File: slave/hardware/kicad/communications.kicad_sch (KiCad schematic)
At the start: 18 parts, among them IC8 L9616, Q2 BSS138, Q3 BSS138, Q4 BSS138, Q5 BSS138

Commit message: feat(HW): add USB Type-C interface
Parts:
- added J1: USB_C_Receptacle_USB2.0_16P, Connector_USB:USB_C_Receptacle_HCTL_HC-TYPE-C-16P-01A, symbol Datalogger:USB_C_Receptacle_USB2.0_16P
- added R71, R73, R74: 20kR, Resistor_SMD:R_0603_1608Metric, symbol Device:R
- added R72: 10kR, Resistor_SMD:R_0603_1608Metric, symbol Device:R
- renumbered C50 to C56, C51 to C57, IC8 to IC12, R11 to R60, R10 to R61, R14 to R62, R15 to R63, R12 to R64, R13 to R65, R16 to R66, R17 to R67, R98 to R68, R99 to R69, R100 to R70
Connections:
- net GNDREF: now also J1.A1 (GND), J1.A12 (GND), J1.B1 (GND), J1.B12 (GND), R71.1, R73.1, R74.1
- new net: J1.A5 (CC1), R73.2
- new net: J1.B5 (CC2), R71.2
- new net: J1.A4 (VBUS), J1.A9 (VBUS), J1.B4 (VBUS), J1.B9 (VBUS), R72.1
- new net USB_D_N: J1.A7 (D-), J1.B7 (D-)
- new net USB_D_P: J1.A6 (D+), J1.B6 (D+)
- new net VBUS: R72.2, R74.2
- no-connect marks 1 -> 4
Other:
- moved on the sheet: C56, C57, IC12, R68, R69, R70

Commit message: feat(HW): add footprints and configure component properties
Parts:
- C56, C57: footprint (none) -> Capacitor_SMD:C_0201_0603Metric
- IC12: footprint SOIC127P600X175-8N -> Datalogger:SOIC127P600X175-8N
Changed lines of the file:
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@@
 			)
 		)
-		(property "Footprint" ""
+		(property "Footprint" "Capacitor_SMD:C_0201_0603Metric"
 			(at 135.89 62.23 0)
 			(hide yes)
@@
 			)
 		)
-		(property "Footprint" ""
+		(property "Footprint" "Capacitor_SMD:C_0201_0603Metric"
 			(at 81.28 49.53 0)
 			(hide yes)
@@
 			)
 		)
-		(property "Footprint" "SOIC127P600X175-8N"
+		(property "Footprint" "Datalogger:SOIC127P600X175-8N"
 			(at 114.3 46.99 0)
 			(hide yes)

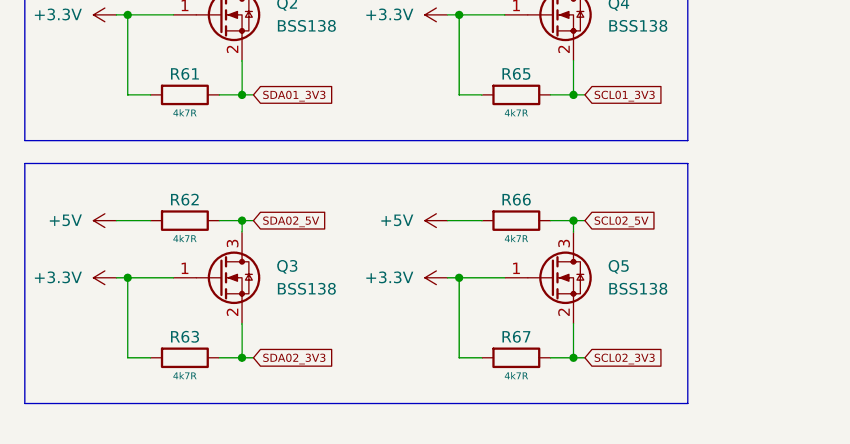
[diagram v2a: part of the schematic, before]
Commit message: feat(HW): add initial schematic pages
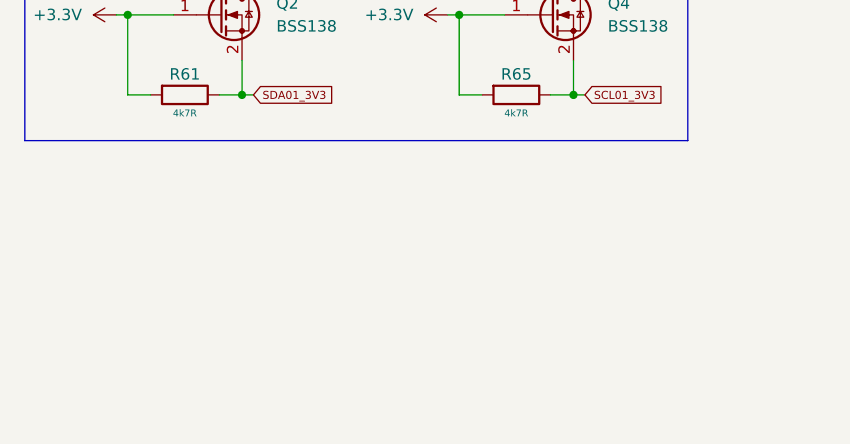
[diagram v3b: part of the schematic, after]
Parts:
- removed Q3, Q5: BSS138, Package_TO_SOT_SMD:SOT-23, symbol Transistor_FET:BSS138
- removed R62, R63, R66, R67: 4k7R, Resistor_SMD:R_0805_2012Metric, symbol Device:R

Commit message: feat(HW): add MCU connections
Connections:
- net CAN_RX: now also IC12.6 (C_L), R70.2
- net CAN_TX: no longer IC12.6 (C_L), R70.2
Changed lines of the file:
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@@
 		)
 	)
-	(global_label "CAN_TX"
+	(global_label "CAN_RX"
 		(shape input)
 		(at 143.51 55.88 0)
@@
 		)
 		(property "Intersheetrefs" "${INTERSHEET_REFS}"
-			(at 150.3831 55.88 0)
+			(at 150.5948 55.88 0)
 			(hide yes)
 			(show_name no)

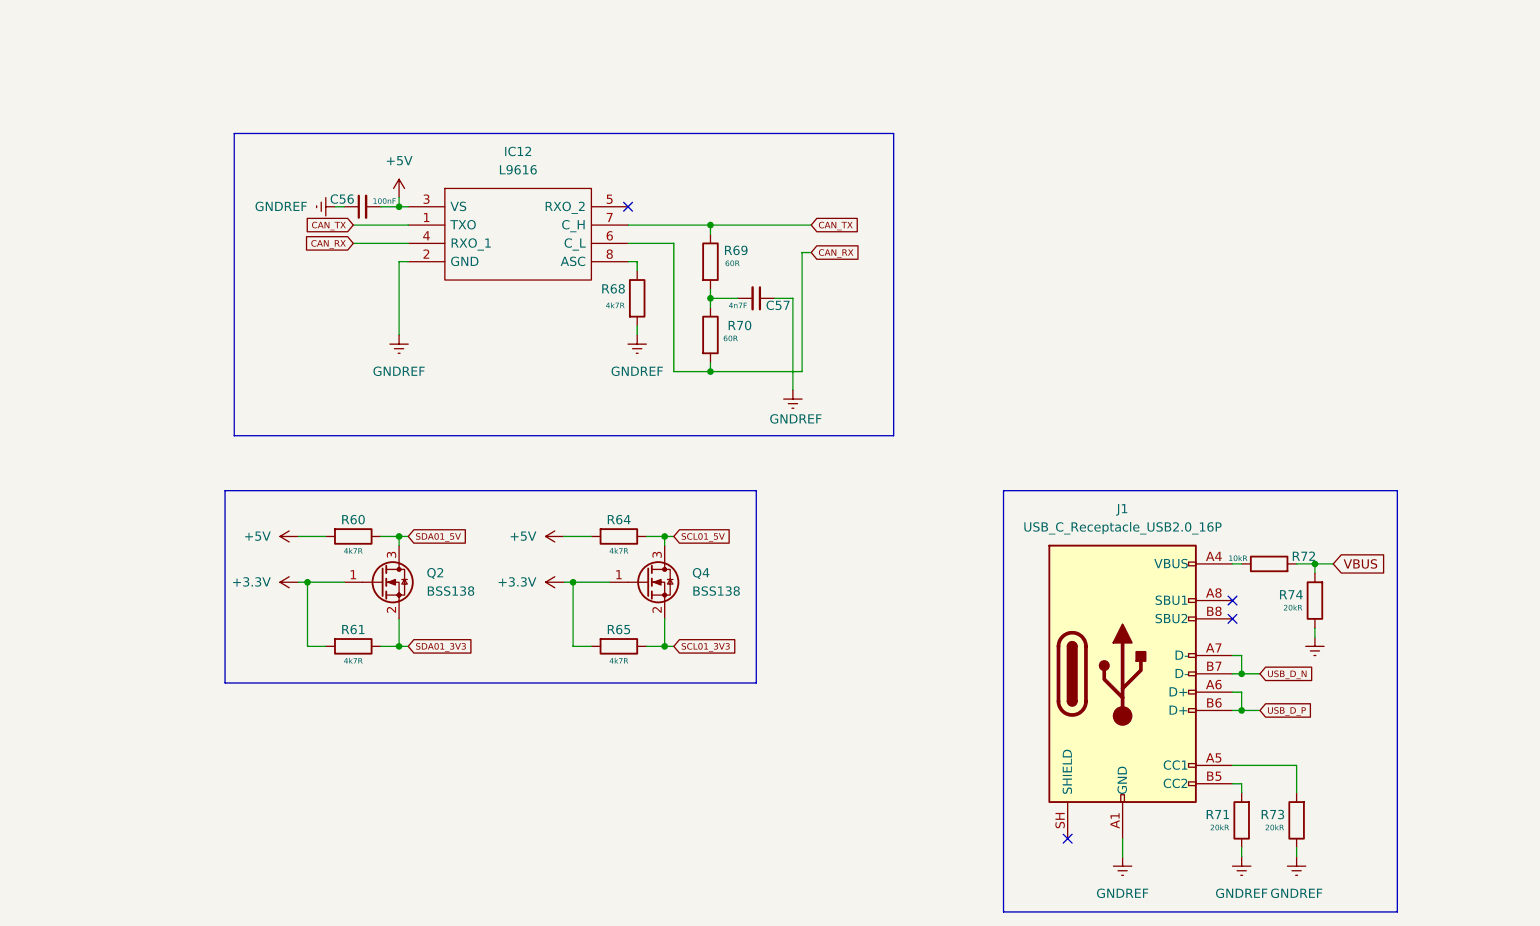
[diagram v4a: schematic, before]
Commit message: feat(HW): add UART communication interface
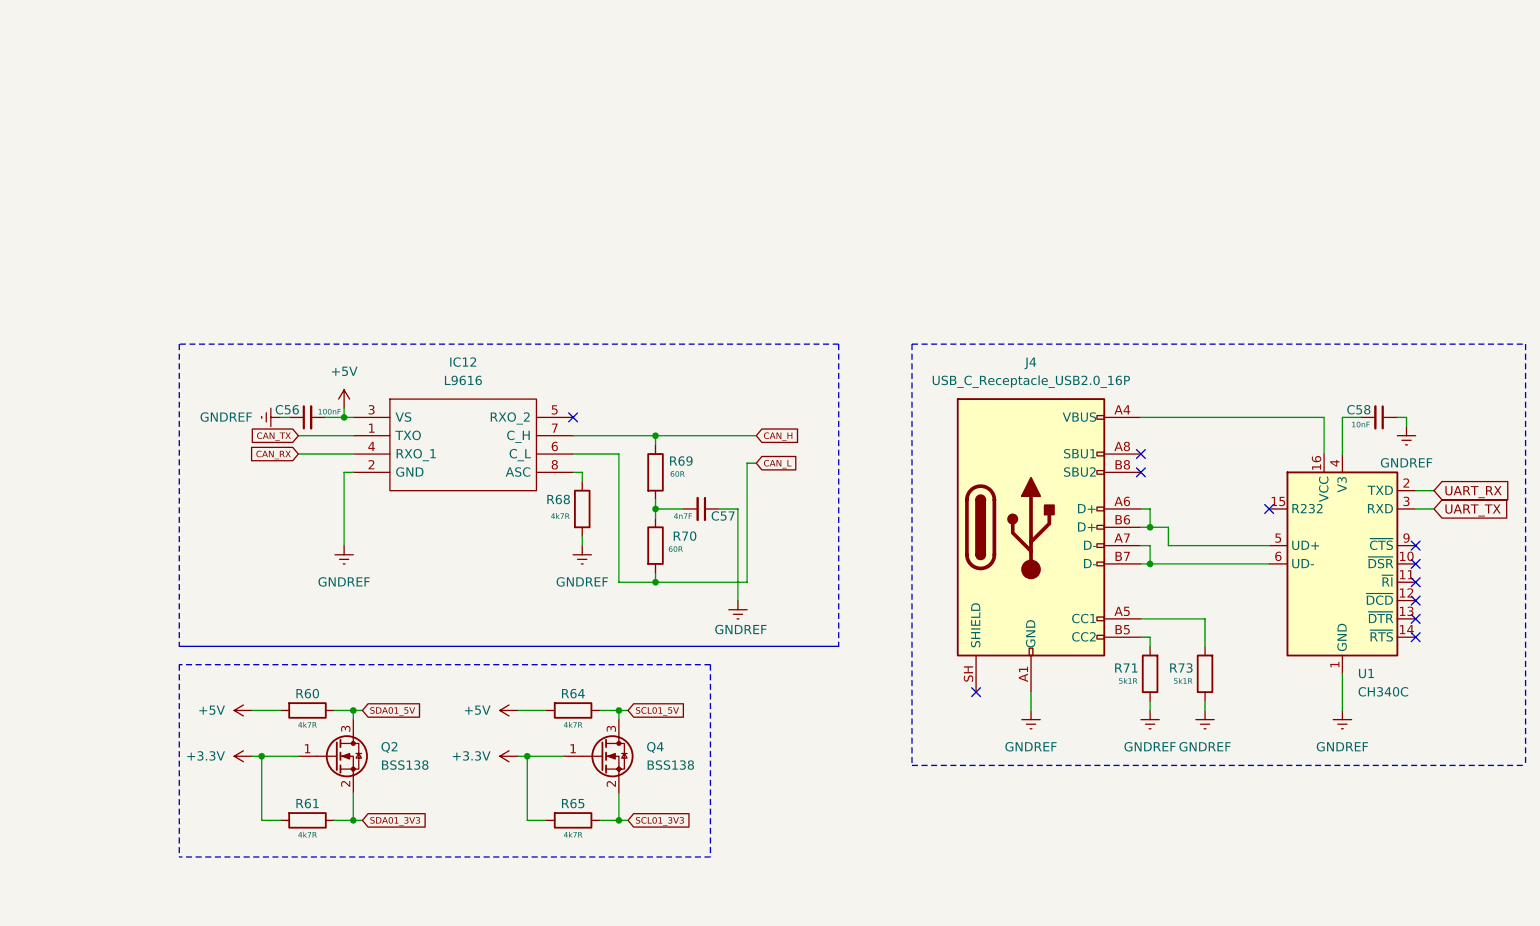
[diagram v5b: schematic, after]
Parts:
- removed J1: USB_C_Receptacle_USB2.0_16P, Connector_USB:USB_C_Receptacle_HCTL_HC-TYPE-C-16P-01A, symbol Datalogger:USB_C_Receptacle_USB2.0_16P
- removed R72: 10kR, Resistor_SMD:R_0603_1608Metric, symbol Device:R
- removed R74: 20kR, Resistor_SMD:R_0603_1608Metric, symbol Device:R
- added C58: 10nF, Capacitor_SMD:C_0201_0603Metric, symbol Device:C_Small
- added J4: USB_C_Receptacle_USB2.0_16P, Connector_USB:USB_C_Receptacle_HCTL_HC-TYPE-C-16P-01A, symbol Datalogger:USB_C_Receptacle_USB2.0_16P
- added U1: CH340C, Package_SO:SOIC-16_3.9x9.9mm_P1.27mm, symbol Interface_USB:CH340C
- R71, R73: value 20kR -> 5k1R
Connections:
- net CAN_RX: no longer IC12.6 (C_L), R70.2
- net CAN_TX: no longer IC12.7 (C_H), R69.1
- net GNDREF: now also C58.1, J4.A1 (GND), J4.A12 (GND), J4.B1 (GND), J4.B12 (GND), U1.1 (GND)
- net at R73.2: now also J4.A5 (CC1)
- net at R71.2: now also J4.B5 (CC2)
- new net: J4.A4 (VBUS), J4.A9 (VBUS), J4.B4 (VBUS), J4.B9 (VBUS), U1.16 (VCC)
- new net: C58.2, U1.4 (V3)
- new net: J4.A6 (D+), J4.B6 (D+), U1.5 (UD+)
- new net: J4.A7 (D-), J4.B7 (D-), U1.6 (UD-)
- new net CAN_H: IC12.7 (C_H), R69.1
- new net CAN_L: IC12.6 (C_L), R70.2
- new net UART_RX: U1.2 (TXD)
- new net UART_TX: U1.3 (RXD)
- no-connect marks 4 -> 11
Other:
- moved on the sheet: C56, C57, IC12, Q2, Q4, R60, R61, R64, R65, R68, R69, R70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
